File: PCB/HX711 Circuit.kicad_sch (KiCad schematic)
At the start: 9 parts, among them U8 Hx711

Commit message: Finish trace routing
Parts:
- C12: renamed from C16; value 0.01U -> U01
- C33: renamed from C35; value C -> U01; footprint (none) -> Capacitor_SMD:C_0805_2012Metric_Pad1.18x1.45mm_HandSolder
- renumbered C15 to C11, R22 to R16, R23 to R17, R24 to R18, TP17 to TP13, TP18 to TP14, U8 to U6
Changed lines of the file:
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@@
   (symbol (lib_id "PCB-rescue:C-Device") (at 121.92 81.28 0)
     (in_bom yes) (on_board yes)
-    (property "Reference" "C15" (id 0) (at 124.841 80.1116 0)
+    (property "Reference" "C11" (id 0) (at 124.841 80.1116 0)
       (effects (font (size 1.27 1.27)) (justify left))
     )
@@
   (symbol (lib_id "Device:C") (at 132.715 81.28 0)
     (in_bom yes) (on_board yes) (fields_autoplaced)
-    (property "Reference" "C35" (id 0) (at 135.636 80.3715 0)
-      (effects (font (size 1.27 1.27)) (justify left))
-    )
-    (property "Value" "C" (id 1) (at 135.636 83.1466 0)
-      (effects (font (size 1.27 1.27)) (justify left))
-    )
-    (property "Footprint" "" (id 2) (at 133.6802 85.09 0)
+    (property "Reference" "C33" (id 0) (at 135.636 80.3715 0)
+      (effects (font (size 1.27 1.27)) (justify left))
+    )
+    (property "Value" "U01" (id 1) (at 135.636 83.1466 0)
+      (effects (font (size 1.27 1.27)) (justify left))
+    )
+    (property "Footprint" "Capacitor_SMD:C_0805_2012Metric_Pad1.18x1.45mm_HandSolder" (id 2) (at 133.6802 85.09 0)
       (effects (font (size 1.27 1.27)) hide)
     )
@@
   (symbol (lib_id "power:GND") (at 114.3 119.38 0)
     (in_bom yes) (on_board yes) (fields_autoplaced)
-    (property "Reference" "#PWR0139" (id 0) (at 114.3 125.73 0)
+    (property "Reference" "#PWR0133" (id 0) (at 114.3 125.73 0)
       (effects (font (size 1.27 1.27)) hide)
     )
@@
   (symbol (lib_id "power:GND") (at 127.635 85.09 0)
     (in_bom yes) (on_board yes)
-    (property "Reference" "#PWR0140" (id 0) (at 127.635 91.44 0)
+    (property "Reference" "#PWR0134" (id 0) (at 127.635 91.44 0)
       (effects (font (size 1.27 1.27)) hide)
     )
@@
   (symbol (lib_id "power:GND") (at 137.16 96.52 0)
     (in_bom yes) (on_board yes)
-    (property "Reference" "#PWR0142" (id 0) (at 137.16 102.87 0)
+    (property "Reference" "#PWR0136" (id 0) (at 137.16 102.87 0)
       (effects (font (size 1.27 1.27)) hide)
     )
@@
   (symbol (lib_id "power:+5V") (at 172.72 76.2 0)
     (in_bom yes) (on_board yes) (fields_autoplaced)
-    (property "Reference" "#PWR0137" (id 0) (at 172.72 80.01 0)
+    (property "Reference" "#PWR0131" (id 0) (at 172.72 80.01 0)
       (effects (font (size 1.27 1.27)) hide)
     )
@@
   (symbol (lib_id "power:GND") (at 114.3 96.52 180)
     (in_bom yes) (on_board yes) (fields_autoplaced)
-    (property "Reference" "#PWR0141" (id 0) (at 114.3 90.17 0)
+    (property "Reference" "#PWR0135" (id 0) (at 114.3 90.17 0)
       (effects (font (size 1.27 1.27)) hide)
     )
@@
   (symbol (lib_id "Connector:TestPoint") (at 107.95 111.76 90)
     (in_bom yes) (on_board yes)
-    (property "Reference" "TP18" (id 0) (at 104.14 114.3 90))
+    (property "Reference" "TP14" (id 0) (at 104.14 114.3 90))
     (property "Value" "TestPoint" (id 1) (at 104.14 116.84 90))
     (property "Footprint" "Custom-footprints:Radial-Pads-With-Relief" (id 2) (at 107.95 106.68 0)
@@
   (symbol (lib_id "Device:R") (at 114.3 100.33 0)
     (in_bom yes) (on_board yes) (fields_autoplaced)
-    (property "Reference" "R22" (id 0) (at 118.11 99.0599 0)
+    (property "Reference" "R16" (id 0) (at 118.11 99.0599 0)
       (effects (font (size 1.27 1.27)) (justify left))
     )
@@
   (symbol (lib_id "PCB-rescue:R-Device") (at 124.46 111.76 270)
     (in_bom yes) (on_board yes)
-    (property "Reference" "R24" (id 0) (at 124.46 106.5022 90))
+    (property "Reference" "R18" (id 0) (at 124.46 106.5022 90))
     (property "Value" "1k" (id 1) (at 124.46 108.8136 90))
     (property "Footprint" "Resistor_SMD:R_0805_2012Metric_Pad1.20x1.40mm_HandSolder" (id 2) (at 124.46 109.982 90)
@@
   (symbol (lib_id "power:GND") (at 172.72 86.36 0)
     (in_bom yes) (on_board yes) (fields_autoplaced)
-    (property "Reference" "#PWR0138" (id 0) (at 172.72 92.71 0)
+    (property "Reference" "#PWR0132" (id 0) (at 172.72 92.71 0)
       (effects (font (size 1.27 1.27)) hide)
     )
@@
   (symbol (lib_id "PCB-rescue:Hx711-HX711-HX711-ADC-rescue") (at 151.13 114.3 0)
     (in_bom yes) (on_board yes)
-    (property "Reference" "U8" (id 0) (at 154.94 68.199 0))
+    (property "Reference" "U6" (id 0) (at 154.94 68.199 0))
     (property "Value" "Hx711" (id 1) (at 154.94 70.5104 0))
     (property "Footprint" "Package_SO:SOIC-16_3.9x9.9mm_P1.27mm" (id 2) (at 154.94 63.5 0)
@@
   (symbol (lib_id "Connector:TestPoint") (at 107.95 104.14 90)
     (in_bom yes) (on_board yes)
-    (property "Reference" "TP17" (id 0) (at 104.14 97.79 90))
+    (property "Reference" "TP13" (id 0) (at 104.14 97.79 90))
     (property "Value" "TestPoint" (id 1) (at 104.14 100.33 90))
     (property "Footprint" "Custom-footprints:Radial-Pads-With-Relief" (id 2) (at 107.95 99.06 0)
@@
   (symbol (lib_id "Device:R") (at 114.3 115.57 180)
     (in_bom yes) (on_board yes)
-    (property "Reference" "R23" (id 0) (at 120.65 116.84 0)
-      (effects (font (size 1.27 1.27)) (justify left))
-    )
-    (property "Value" "350" (id 1) (at 121.92 114.3 0)
+    (property "Reference" "R17" (id 0) (at 120.65 116.84 0)
+      (effects (font (size 1.27 1.27)) (justify left))
+    )
+    (property "Value" "350" (id 1) (at 120.65 114.3 0)
       (effects (font (size 1.27 1.27)) (justify left))
     )
@@
   (symbol (lib_id "PCB-rescue:C-Device") (at 130.81 107.95 0)
     (in_bom yes) (on_board yes)
-    (property "Reference" "C16" (id 0) (at 133.731 106.7816 0)
-      (effects (font (size 1.27 1.27)) (justify left))
-    )
-    (property "Value" "0.01U" (id 1) (at 133.731 109.093 0)
-      (effects (font (size 1.27 1.27)) (justify left))
-    )
+    (property "Reference" "C12" (id 0) (at 133.731 106.7816 0)
+      (effects (font (size 1.27 1.27)) (justify left))
+    )
+    (property "Value" "U01" (id 1) (at 133.731 109.093 0)
+      (effects (font (size 1.27 1.27)) (justify left))
+    )

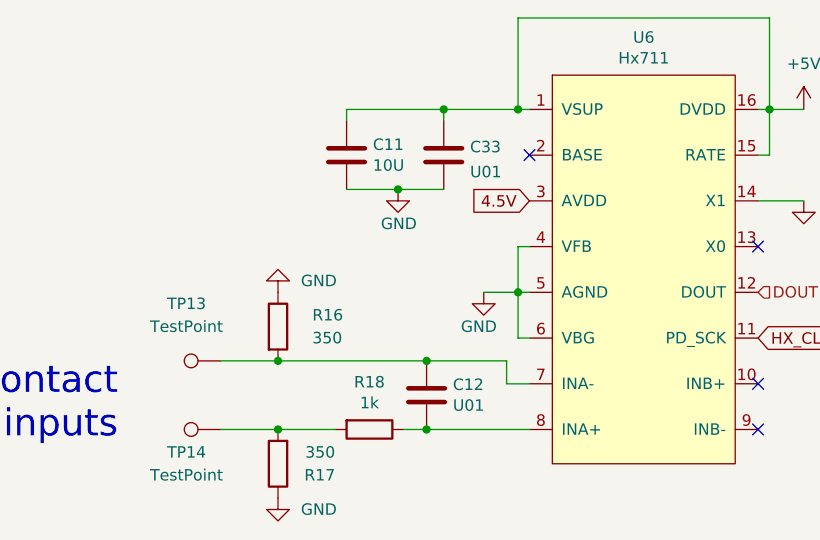
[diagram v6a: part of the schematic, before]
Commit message: Fix _CE so it is now LOW
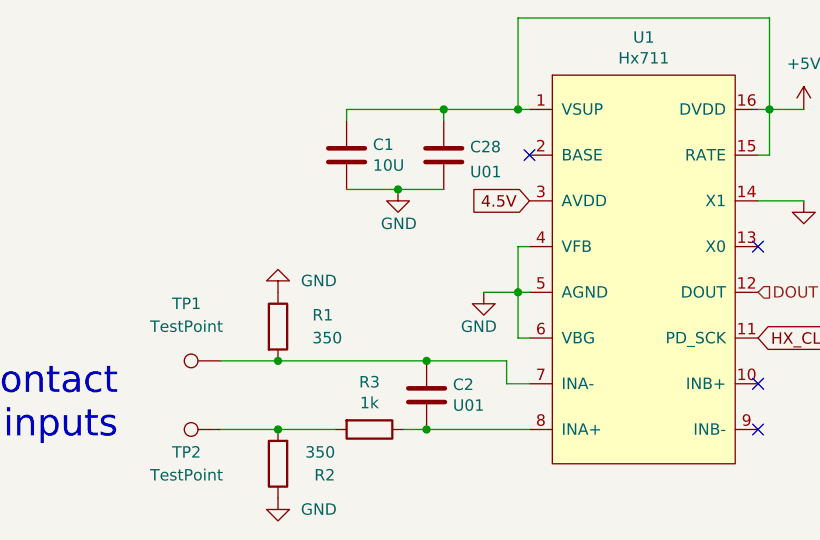
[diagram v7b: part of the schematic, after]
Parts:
- renumbered C11 to C1, C12 to C2, C33 to C28, R16 to R1, R17 to R2, R18 to R3, TP13 to TP1, TP14 to TP2, U6 to U1

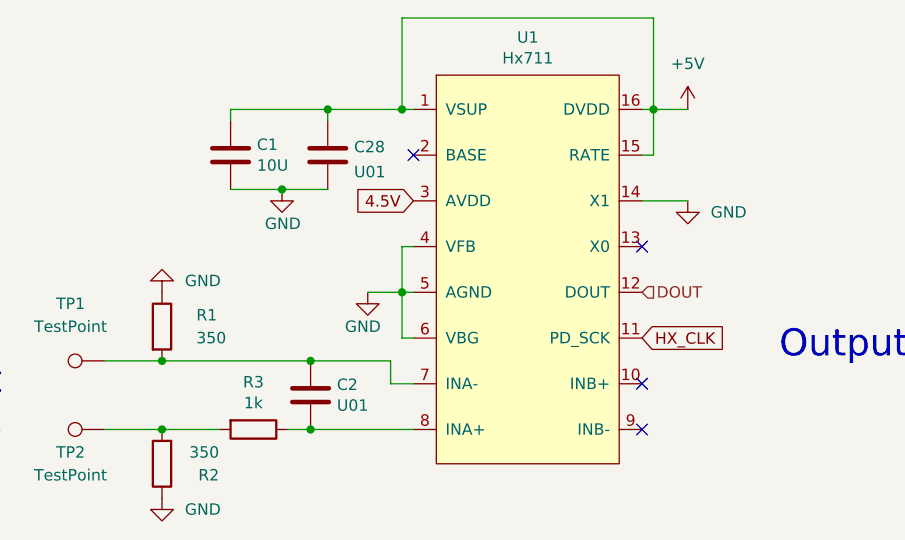
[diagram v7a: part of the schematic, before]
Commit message: Switch VDD to 3.3V. Ready for comp
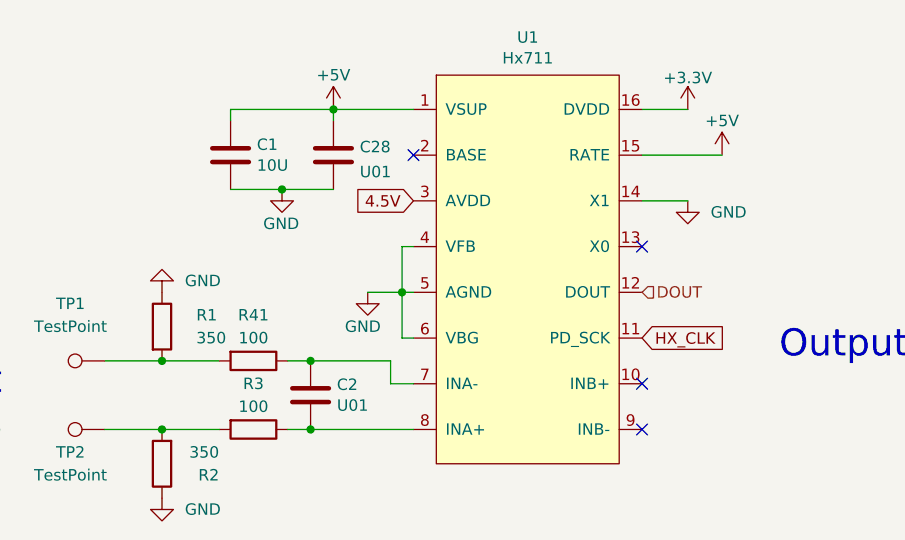
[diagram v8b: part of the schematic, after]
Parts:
- added R41: 100, Resistor_SMD:R_0805_2012Metric_Pad1.20x1.40mm_HandSolder, symbol PCB-rescue:R-Device
- R3: value 1k -> 100
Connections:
- net +5V: no longer U1.16 (DVDD)
- net at C2.1, U1.7 (INA-): now also R41.1; no longer R1.2, TP1.1
- new net: R1.2, R41.2, TP1.1
- new net +3.3V: U1.16 (DVDD)
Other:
- moved on the sheet: C28
